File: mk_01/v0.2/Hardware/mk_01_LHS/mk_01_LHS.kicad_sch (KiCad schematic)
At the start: 45 parts, among them SW1 SW_Push_Dual, U1 nice_nano

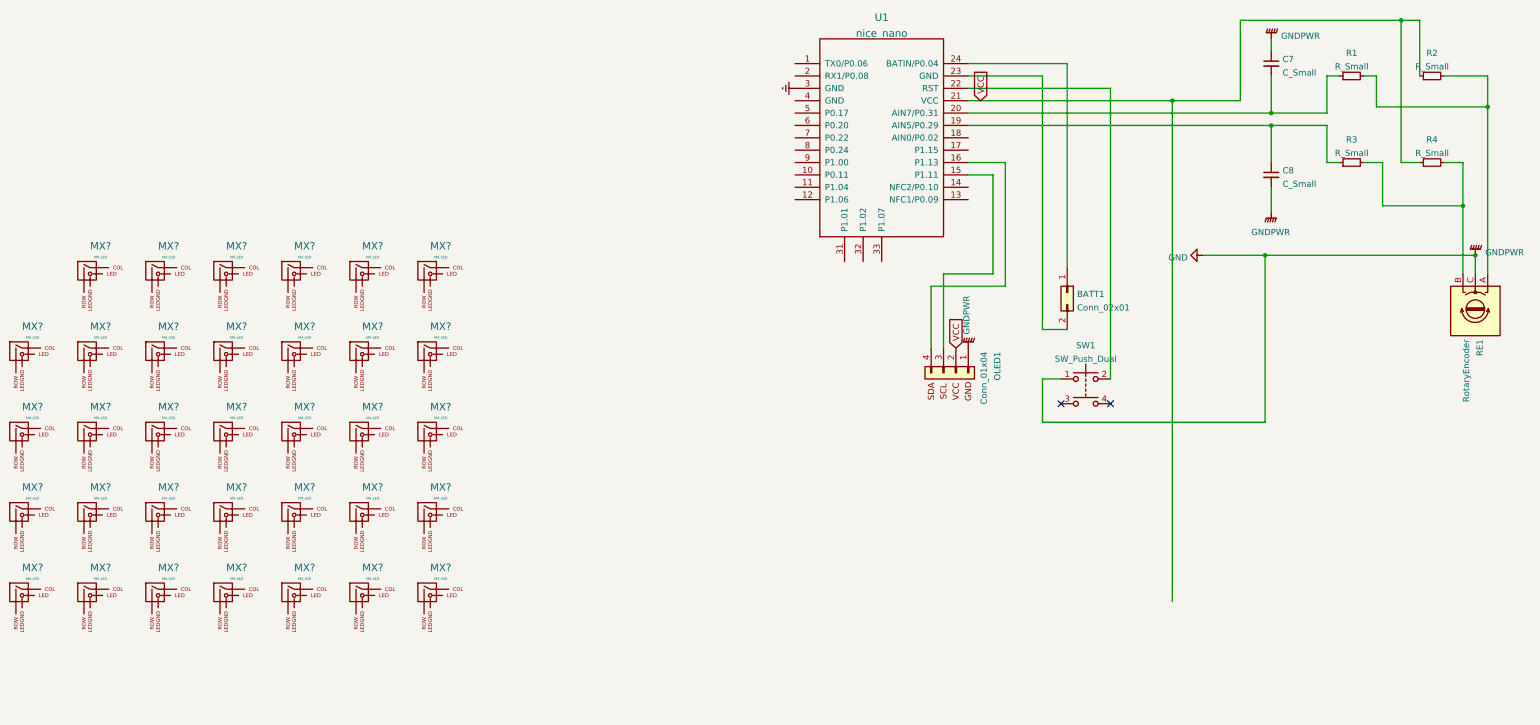
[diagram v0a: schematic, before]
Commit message: Hardware updates
Keyboard matrix is complete, on both the schematic and the board design. To keep the design simple, I will remove the LEDs.
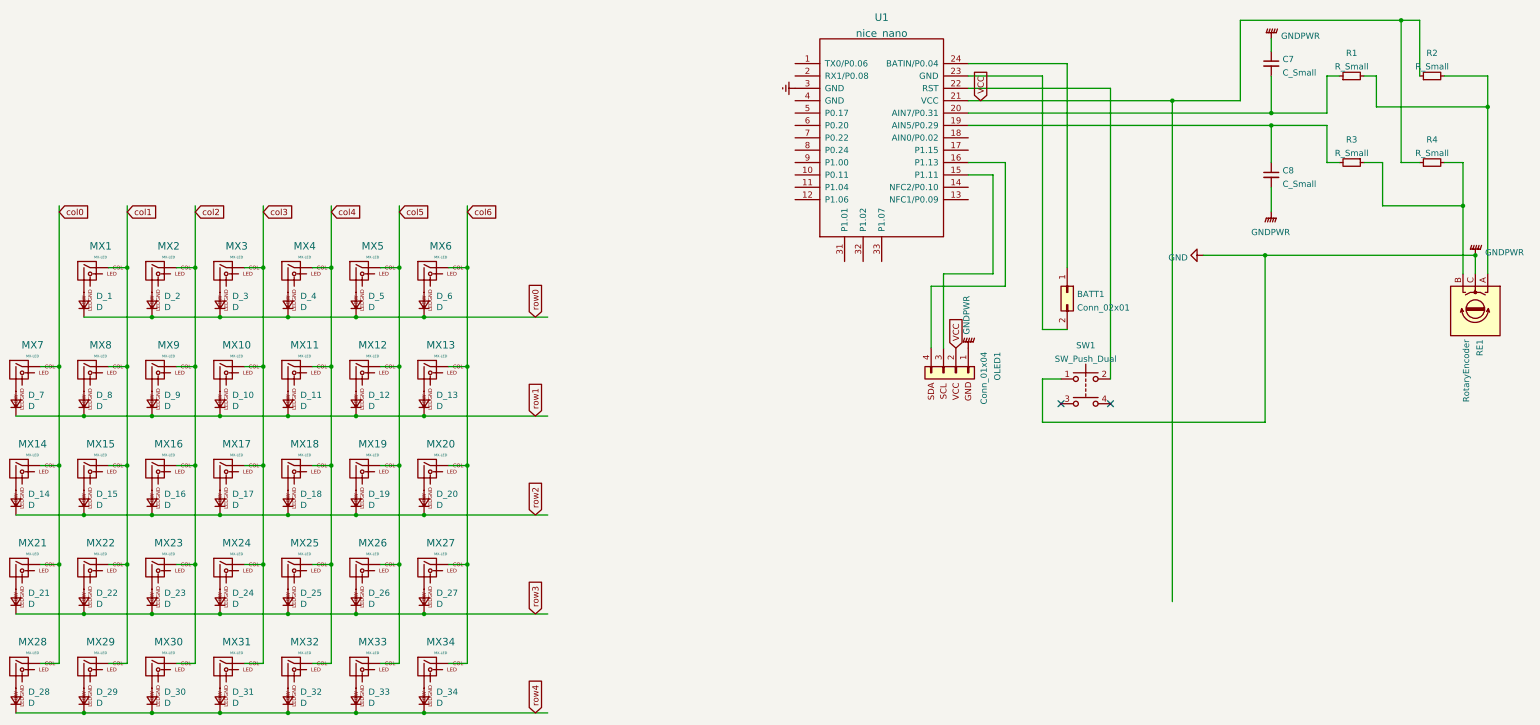
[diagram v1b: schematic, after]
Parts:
- added D_1, D_10, D_11, D_12, D_13, D_14, D_15, D_16, D_17, D_18, D_19, D_2, D_20, D_21, D_22, D_23, D_24, D_25, D_26, D_27, D_28, D_29, D_3, D_30, D_31, D_32, D_33, D_34, D_4, D_5, D_6, D_7, D_8, D_9: D, Diode_SMD:D_SOD-123, symbol Device:D_Small
- C7, C8: footprint Capacitor_SMD:C_0402_1005Metric_Pad0.74x0.62mm_HandSolder -> Capacitor_SMD:C_0805_2012Metric_Pad1.18x1.45mm_HandSolder
- R1, R2, R3, R4: footprint Resistor_SMD:R_0201_0603Metric_Pad0.64x0.40mm_HandSolder -> Resistor_SMD:R_0805_2012Metric_Pad1.20x1.40mm_HandSolder
- gave numbers to parts that had none: 34
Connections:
- net col4: now reaches MX11.1 (COL)
- net col4: now also MX18.1 (COL), MX25.1 (COL), MX32.1 (COL), MX4.1 (COL)
- net at MX11.2 (ROW): now also D_11.2 (A)
- net col0: now reaches MX7.1 (COL)
- net col0: now also MX14.1 (COL), MX21.1 (COL), MX28.1 (COL)
- net at MX7.2 (ROW): now also D_7.2 (A)
- net col1: now reaches MX29.1 (COL)
- net col1: now also MX1.1 (COL), MX15.1 (COL), MX22.1 (COL), MX8.1 (COL)
- net at MX29.2 (ROW): now also D_29.2 (A)
- net col3: now reaches MX3.1 (COL)
- net col3: now also MX10.1 (COL), MX17.1 (COL), MX24.1 (COL), MX31.1 (COL)
- net at MX3.2 (ROW): now also D_3.2 (A)
- net at MX17.2 (ROW): now also D_17.2 (A)
- net at MX15.2 (ROW): now also D_15.2 (A)
- net at R4.2, RE1.B: now also R3.1; no longer R3.2
- net at C8.1, U1.19 (AIN5/P0.29): now also R3.2; no longer R3.1
- net col2: now reaches MX2.1 (COL)
- net col2: now also MX16.1 (COL), MX23.1 (COL), MX30.1 (COL), MX9.1 (COL)
- net at MX2.2 (ROW): now also D_2.2 (A)
- net at MX8.2 (ROW): now also D_8.2 (A)
- net col5: now reaches MX12.1 (COL)
- net col5: now also MX19.1 (COL), MX26.1 (COL), MX33.1 (COL), MX5.1 (COL)
- net at MX12.2 (ROW): now also D_12.2 (A)
- net at MX10.2 (ROW): now also D_10.2 (A)
- net at MX9.2 (ROW): now also D_9.2 (A)
- net at MX30.2 (ROW): now also D_30.2 (A)
- net at MX18.2 (ROW): now also D_18.2 (A)
- net col6: now reaches MX27.1 (COL)
- net col6: now also MX13.1 (COL), MX20.1 (COL), MX34.1 (COL), MX6.1 (COL)
- net at MX27.2 (ROW): now also D_27.2 (A)
- net at MX33.2 (ROW): now also D_33.2 (A)
- net at MX19.2 (ROW): now also D_19.2 (A)
- net at MX34.2 (ROW): now also D_34.2 (A)
- net at MX26.2 (ROW): now also D_26.2 (A)
- net at MX24.2 (ROW): now also D_24.2 (A)
- net at MX23.2 (ROW): now also D_23.2 (A)
- net at MX25.2 (ROW): now also D_25.2 (A)
- net at MX16.2 (ROW): now also D_16.2 (A)
- net at MX20.2 (ROW): now also D_20.2 (A)
- net at MX5.2 (ROW): now also D_5.2 (A)
- net at MX32.2 (ROW): now also D_32.2 (A)
- net at MX4.2 (ROW): now also D_4.2 (A)
- net at MX14.2 (ROW): now also D_14.2 (A)
- net at MX28.2 (ROW): now also D_28.2 (A)
- net at MX1.2 (ROW): now also D_1.2 (A)
- net at MX22.2 (ROW): now also D_22.2 (A)
- net at MX13.2 (ROW): now also D_13.2 (A)
- net at MX21.2 (ROW): now also D_21.2 (A)
- net at MX6.2 (ROW): now also D_6.2 (A)
- net at MX31.2 (ROW): now also D_31.2 (A)
- new net row0: D_1.1 (K), D_2.1 (K), D_3.1 (K), D_4.1 (K), D_5.1 (K), D_6.1 (K)
- new net row1: D_10.1 (K), D_11.1 (K), D_12.1 (K), D_13.1 (K), D_7.1 (K), D_8.1 (K), D_9.1 (K)
- new net row2: D_14.1 (K), D_15.1 (K), D_16.1 (K), D_17.1 (K), D_18.1 (K), D_19.1 (K), D_20.1 (K)
- new net row3: D_21.1 (K), D_22.1 (K), D_23.1 (K), D_24.1 (K), D_25.1 (K), D_26.1 (K), D_27.1 (K)
- new net row4: D_28.1 (K), D_29.1 (K), D_30.1 (K), D_31.1 (K), D_32.1 (K), D_33.1 (K), D_34.1 (K)
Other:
- moved on the sheet: MX10, MX11, MX12, MX13, MX14, MX15, MX16, MX17, MX18, MX19, MX20, MX21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
